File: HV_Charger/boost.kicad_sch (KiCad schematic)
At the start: 9 parts

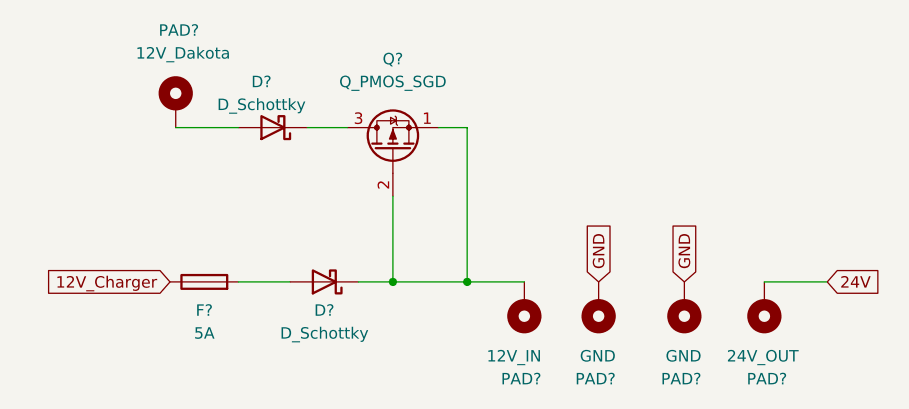
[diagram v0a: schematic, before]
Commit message: Fixed Rylan issues, pls switch diodes on pmos
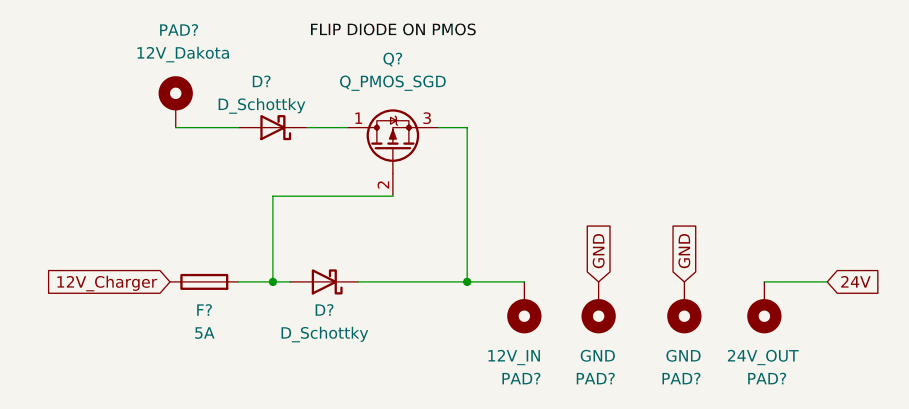
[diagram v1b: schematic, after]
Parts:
- Q?: footprint (none) -> SamacSys_Parts:BTS3035TFATMA1; symbol Device:Q_PMOS_SGD -> Device:Q_PMOS_DGS
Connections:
- net at D?.1 (K), PAD?.1: now also Q?.3 (S); no longer Q?.1 (S), Q?.2 (G)
- net at D?.1 (K): now also Q?.1 (D); no longer Q?.3 (D)
- net at D?.2 (A), F?.2: now also Q?.2 (G)
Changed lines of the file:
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@@
   (junction (at 139.7 85.09) (diameter 0) (color 0 0 0 0)
   )
-  (junction (at 131.445 85.09) (diameter 0) (color 0 0 0 0)
+  (junction (at 118.11 85.09) (diameter 0) (color 0 0 0 0)
   )
   (wire (pts (xy 139.7 85.09) (xy 146.05 85.09))
@@
     (stroke (width 0) (type default) (color 0 0 0 0))
   )
-  (wire (pts (xy 127.635 85.09) (xy 131.445 85.09))
-    (stroke (width 0) (type default) (color 0 0 0 0))
-  )
-  (wire (pts (xy 114.3 85.09) (xy 120.015 85.09))
-    (stroke (width 0) (type default) (color 0 0 0 0))
-  )
-  (wire (pts (xy 131.445 75.565) (xy 131.445 85.09))
+  (wire (pts (xy 114.3 85.09) (xy 118.11 85.09))
     (stroke (width 0) (type default) (color 0 0 0 0))
   )
   (wire (pts (xy 121.92 67.945) (xy 126.365 67.945))
+    (stroke (width 0) (type default) (color 0 0 0 0))
+  )
+  (wire (pts (xy 118.11 75.565) (xy 118.11 85.09))
     (stroke (width 0) (type default) (color 0 0 0 0))
   )
@@
     (stroke (width 0) (type default) (color 0 0 0 0))
   )
+  (wire (pts (xy 118.11 85.09) (xy 120.015 85.09))
+    (stroke (width 0) (type default) (color 0 0 0 0))
+  )
+  (wire (pts (xy 131.445 75.565) (xy 118.11 75.565))
+    (stroke (width 0) (type default) (color 0 0 0 0))
+  )
   (wire (pts (xy 136.525 67.945) (xy 139.7 67.945))
     (stroke (width 0) (type default) (color 0 0 0 0))
   )
-  (wire (pts (xy 131.445 85.09) (xy 139.7 85.09))
+  (wire (pts (xy 127.635 85.09) (xy 139.7 85.09))
     (stroke (width 0) (type default) (color 0 0 0 0))
+  )
+  (label "FLIP DIODE ON PMOS" (at 122.174 58.166 0)
+    (effects (font (size 1.27 1.27)) (justify left bottom))
   )
   (global_label "GND" (shape input) (at 163.83 85.09 90) (fields_autoplaced)
@@
     (pin "1")
   )
-  (symbol (lib_id "Device:Q_PMOS_SGD") (at 131.445 70.485 90) (unit 1)
+  (symbol (lib_id "Device:Q_PMOS_DGS") (at 131.445 70.485 90) (unit 1)
     (in_bom yes) (on_board yes) (fields_autoplaced)
     (property "Reference" "Q?" (id 0) (at 131.445 60.325 90))
     (property "Value" "Q_PMOS_SGD" (id 1) (at 131.445 62.865 90))
-    (property "Footprint" "" (id 2) (at 128.905 65.405 0)
+    (property "Footprint" "SamacSys_Parts:BTS3035TFATMA1" (id 2) (at 128.905 65.405 0)
       (effects (font (size 1.27 1.27)) hide)
     )
-    (property "Datasheet" "~https://www.mouser.com/ProductDetail/Infineon-Technologies/IPD650P06NMATMA1?qs=unwgFEO1A6vz3T2Vr47kIg%3D%3D" (id 3) (at 131.445 70.485 0)
+    (property "Datasheet" "~" (id 3) (at 131.445 70.485 0)
       (effects (font (size 1.27 1.27)) hide)
     )
